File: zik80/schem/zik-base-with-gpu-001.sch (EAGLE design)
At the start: 5 parts, among them IC1 TPS7133QP, IC2 7805TV

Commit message: import eagle libs; update base schematic
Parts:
- added U$1: DCJACKZIK, skeezix:DCJACKZIK
- added U$2: TOGGLE-CYAN-L-ZIK, skeezix:TOGGLE-CYAN-L-ZIK
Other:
- note added: "- header for power supply direct feed - header for output 9v, 5v, 3.3v"
- note removed: "TODO: - Vcc Vss Posts - DC jack"
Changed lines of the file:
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@@
 <part name="GND5" library="supply1" deviceset="GND" device=""/>
 <part name="P+3" library="supply1" deviceset="VCC" device=""/>
+<part name="U$1" library="skeezix" deviceset="DCJACKZIK" device=""/>
+<part name="U$2" library="skeezix" deviceset="TOGGLE-CYAN-L-ZIK" device=""/>
+<part name="P+5" library="supply1" deviceset="VCC" device=""/>
+<part name="GND6" library="supply1" deviceset="GND" device=""/>
 </parts>
 <sheets>
@@
 <text x="73.66" y="44.45" size="1.778" layer="91">5V-&gt;3.3V regulator</text>
 <text x="2.54" y="24.13" size="1.778" layer="91">VCC 9V-&gt;5V regulator</text>
-<text x="12.7" y="39.37" size="2.54" layer="94">TODO:
-- Vcc Vss Posts
-- DC jack</text>
+<text x="-5.08" y="41.91" size="2.54" layer="94">- header for power supply direct feed
+- header for output 9v, 5v, 3.3v</text>
 </plain>
 <instances>
@@
 <instance part="GND5" gate="1" x="63.5" y="3.81" rot="R90"/>
 <instance part="P+3" gate="VCC" x="-5.08" y="20.32" rot="R90"/>
+<instance part="U$1" gate="G$1" x="2.54" y="-12.7"/>
+<instance part="U$2" gate="G$1" x="50.8" y="-15.24" rot="R90"/>
+<instance part="P+5" gate="VCC" x="67.31" y="-6.35" rot="R270"/>
+<instance part="GND6" gate="1" x="64.77" y="-17.78"/>
 </instances>
 <busses>
@@
 <junction x="8.89" y="3.81"/>
 </segment>
+<segment>
+<wire x1="54.61" y1="-13.97" x2="64.77" y2="-13.97" width="0.1524" layer="91"/>
+<wire x1="64.77" y1="-13.97" x2="64.77" y2="-15.24" width="0.1524" layer="91"/>
+<pinref part="GND6" gate="1" pin="GND"/>
+</segment>
 </net>
 <net name="+3V3" class="0">
@@
 <pinref part="P+3" gate="VCC" pin="VCC"/>
 </segment>
+<segment>
+<wire x1="54.61" y1="-6.35" x2="64.77" y2="-6.35" width="0.1524" layer="91"/>
+<pinref part="P+5" gate="VCC" pin="VCC"/>
+</segment>
 </net>
+<net name="N$1" class="0">
+<segment>
+<wire x1="19.05" y1="-7.62" x2="19.05" y2="-6.35" width="0.1524" layer="91"/>
+<wire x1="19.05" y1="-6.35" x2="36.83" y2="-6.35" width="0.1524" layer="91"/>
+<junction x="36.83" y="-6.35"/>
+<junction x="19.05" y="-7.62"/>
+</segment>
+</net>
+<net name="N$2" class="0">
+<segment>
+<wire x1="19.05" y1="-10.16" x2="19.05" y2="-13.97" width="0.1524" layer="91"/>
+<wire x1="19.05" y1="-13.97" x2="36.83" y2="-13.97" width="0.1524" layer="91"/>
+<junction x="36.83" y="-13.97"/>
+<junction x="19.05" y="-10.16"/>
+</segment>
+</net>

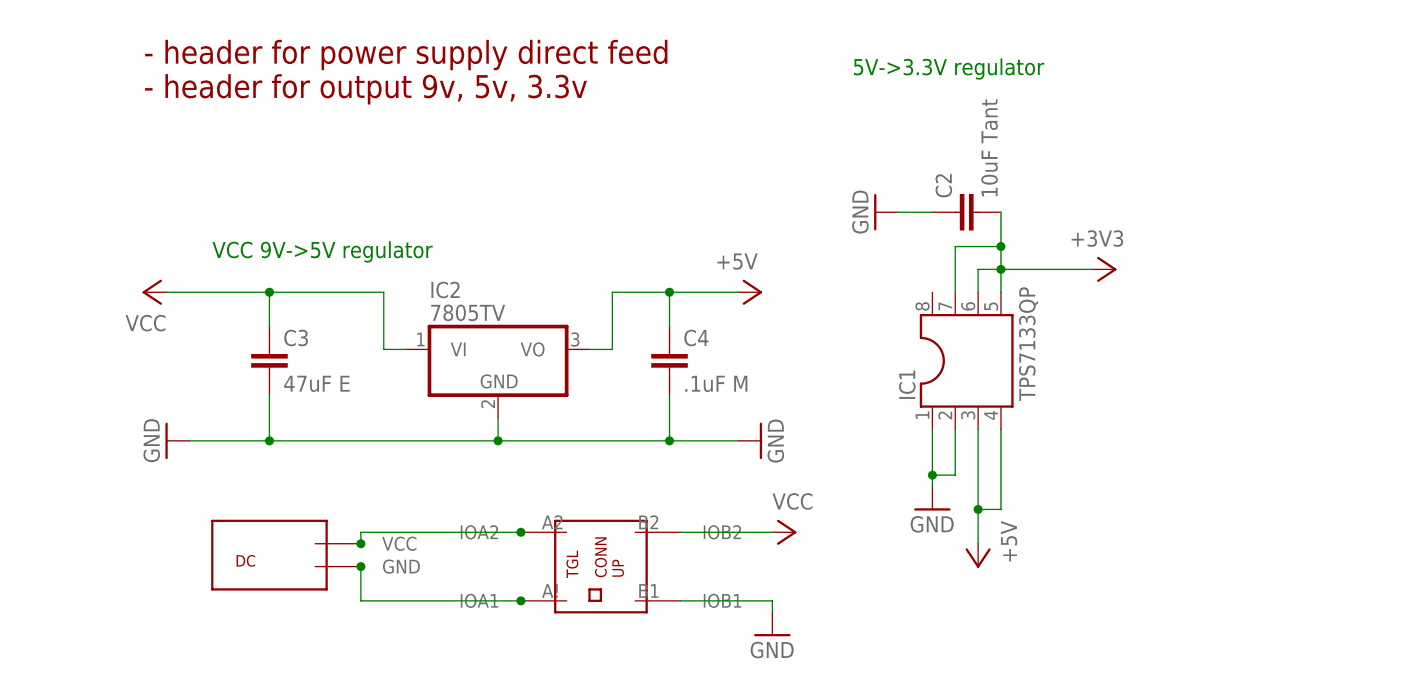
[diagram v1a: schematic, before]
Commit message: Added pinheaders to power section of board
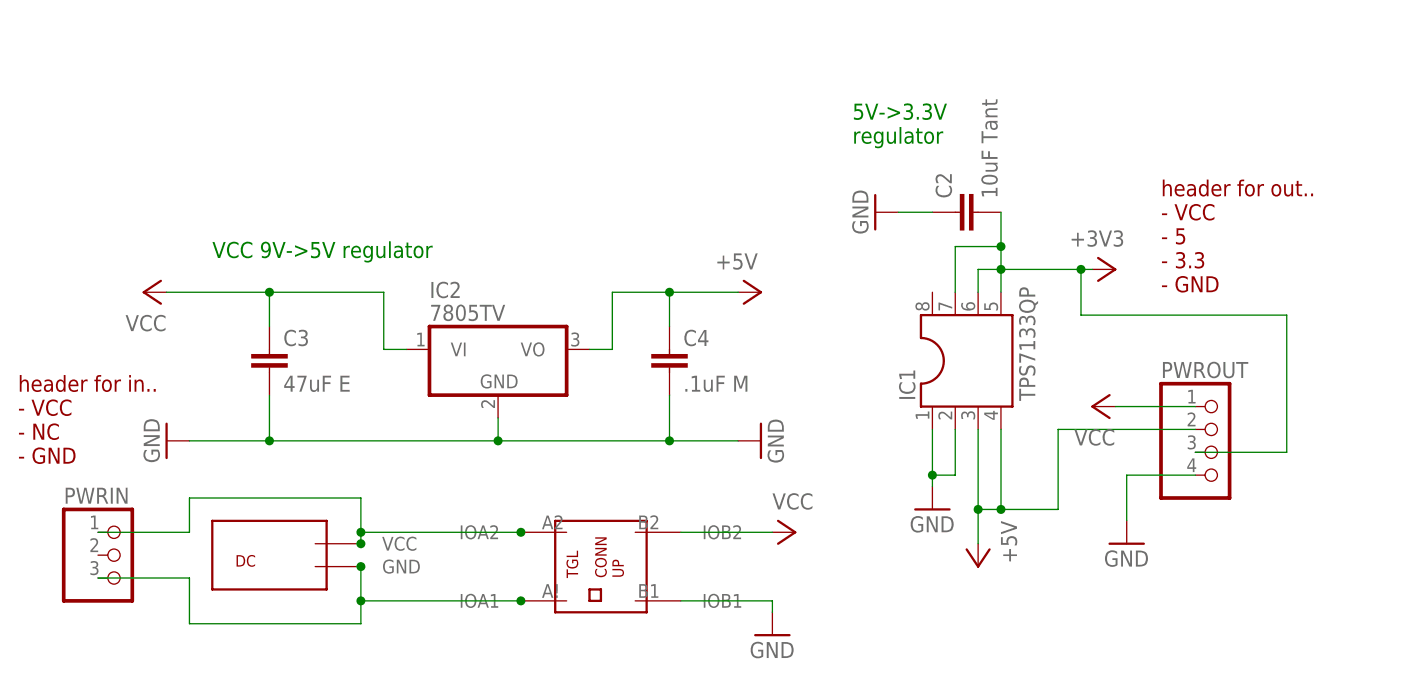
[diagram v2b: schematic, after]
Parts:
- added PWRIN: (no value), pinhead:PINHD-1X3
- added PWROUT: (no value), pinhead:PINHD-1X4
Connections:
- new net N$1: PWRIN.1
- new net N$2: PWRIN.3
- net +3V3: now also PWROUT.3
- net +5V: now also PWROUT.2
- net GND: now also PWROUT.4
- net VCC: now also PWROUT.1
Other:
- note added: "header for in.. - VCC - NC - GND"
- note added: "header for out.. - VCC - 5 - 3.3 - GND"
- note removed: "- header for power supply direct feed - header for output 9v, 5v, 3.3v"
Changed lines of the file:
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@@
 <part name="P+5" library="supply1" deviceset="VCC" device=""/>
 <part name="GND6" library="supply1" deviceset="GND" device=""/>
+<part name="PWRIN" library="pinhead" deviceset="PINHD-1X3" device=""/>
+<part name="PWROUT" library="pinhead" deviceset="PINHD-1X4" device=""/>
+<part name="GND1" library="supply1" deviceset="GND" device=""/>
+<part name="P+1" library="supply1" deviceset="VCC" device=""/>
 </parts>
 <sheets>
 <sheet>
 <plain>
-<text x="73.66" y="44.45" size="1.778" layer="91">5V-&gt;3.3V regulator</text>
+<text x="73.66" y="36.83" size="1.778" layer="91">5V-&gt;3.3V
+regulator</text>
 <text x="2.54" y="24.13" size="1.778" layer="91">VCC 9V-&gt;5V regulator</text>
-<text x="-5.08" y="41.91" size="2.54" layer="94">- header for power supply direct feed
-- header for output 9v, 5v, 3.3v</text>
+<text x="107.95" y="20.32" size="1.778" layer="94">header for out..
+- VCC
+- 5
+- 3.3
+- GND</text>
+<text x="-19.05" y="1.27" size="1.778" layer="94">header for in..
+- VCC
+- NC
+- GND</text>
 </plain>
 <instances>
@@
 <instance part="P+5" gate="VCC" x="67.31" y="-6.35" rot="R270"/>
 <instance part="GND6" gate="1" x="64.77" y="-17.78"/>
+<instance part="PWRIN" gate="A" x="-7.62" y="-8.89"/>
+<instance part="PWROUT" gate="A" x="114.3" y="2.54"/>
+<instance part="GND1" gate="1" x="104.14" y="-7.62"/>
+<instance part="P+1" gate="VCC" x="100.33" y="7.62" rot="R90"/>
 </instances>
 <busses>
@@
 <wire x1="90.17" y1="-3.81" x2="87.63" y2="-3.81" width="0.1524" layer="91"/>
 <junction x="87.63" y="-3.81"/>
+<wire x1="90.17" y1="-3.81" x2="96.52" y2="-3.81" width="0.1524" layer="91"/>
+<wire x1="96.52" y1="-3.81" x2="96.52" y2="5.08" width="0.1524" layer="91"/>
+<junction x="90.17" y="-3.81"/>
+<pinref part="PWROUT" gate="A" pin="2"/>
+<wire x1="96.52" y1="5.08" x2="111.76" y2="5.08" width="0.1524" layer="91"/>
 </segment>
 <segment>
@@
 <pinref part="GND6" gate="1" pin="GND"/>
 </segment>
+<segment>
+<pinref part="PWROUT" gate="A" pin="4"/>
+<wire x1="111.76" y1="0" x2="104.14" y2="0" width="0.1524" layer="91"/>
+<wire x1="104.14" y1="0" x2="104.14" y2="-5.08" width="0.1524" layer="91"/>
+<pinref part="GND1" gate="1" pin="GND"/>
+</segment>
 </net>
 <net name="+3V3" class="0">
@@
 <wire x1="87.63" y1="22.86" x2="87.63" y2="20.32" width="0.1524" layer="91"/>
 <junction x="90.17" y="22.86"/>
-<wire x1="90.17" y1="22.86" x2="100.33" y2="22.86" width="0.1524" layer="91"/>
+<wire x1="90.17" y1="22.86" x2="99.06" y2="22.86" width="0.1524" layer="91"/>
 <pinref part="+3V1" gate="G$1" pin="+3V3"/>
+<wire x1="99.06" y1="22.86" x2="100.33" y2="22.86" width="0.1524" layer="91"/>
+<wire x1="99.06" y1="22.86" x2="99.06" y2="17.78" width="0.1524" layer="91"/>
+<wire x1="99.06" y1="17.78" x2="121.92" y2="17.78" width="0.1524" layer="91"/>
+<wire x1="121.92" y1="17.78" x2="121.92" y2="2.54" width="0.1524" layer="91"/>
+<junction x="99.06" y="22.86"/>
+<pinref part="PWROUT" gate="A" pin="3"/>
+<wire x1="121.92" y1="2.54" x2="111.76" y2="2.54" width="0.1524" layer="91"/>
 </segment>
 </net>
@@
 <pinref part="P+5" gate="VCC" pin="VCC"/>
 </segment>
+<segment>
+<pinref part="PWROUT" gate="A" pin="1"/>
+<wire x1="111.76" y1="7.62" x2="102.87" y2="7.62" width="0.1524" layer="91"/>
+<pinref part="P+1" gate="VCC" pin="VCC"/>
+</segment>
 </net>
 <net name="N$1" class="0">
@@
 <junction x="36.83" y="-6.35"/>
 <junction x="19.05" y="-7.62"/>
+<pinref part="PWRIN" gate="A" pin="1"/>
+<wire x1="-10.16" y1="-6.35" x2="0" y2="-6.35" width="0.1524" layer="91"/>
+<wire x1="0" y1="-6.35" x2="0" y2="-2.54" width="0.1524" layer="91"/>
+<wire x1="0" y1="-2.54" x2="19.05" y2="-2.54" width="0.1524" layer="91"/>
+<wire x1="19.05" y1="-2.54" x2="19.05" y2="-6.35" width="0.1524" layer="91"/>
+<junction x="19.05" y="-6.35"/>
 </segment>
 </net>
@@
 <junction x="36.83" y="-13.97"/>
 <junction x="19.05" y="-10.16"/>
+<pinref part="PWRIN" gate="A" pin="3"/>
+<wire x1="-10.16" y1="-11.43" x2="0" y2="-11.43" width="0.1524" layer="91"/>
+<wire x1="0" y1="-11.43" x2="0" y2="-16.51" width="0.1524" layer="91"/>
+<wire x1="0" y1="-16.51" x2="19.05" y2="-16.51" width="0.1524" layer="91"/>
+<wire x1="19.05" y1="-16.51" x2="19.05" y2="-13.97" width="0.1524" layer="91"/>
+<junction x="19.05" y="-13.97"/>
 </segment>
 </net>
